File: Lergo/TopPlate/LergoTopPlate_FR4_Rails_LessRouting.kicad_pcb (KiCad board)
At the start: 2 copper layers, 164 x 146.3 mm, 74 parts, among them SW2 KEY_SWITCH, SW2 PRO MICRO

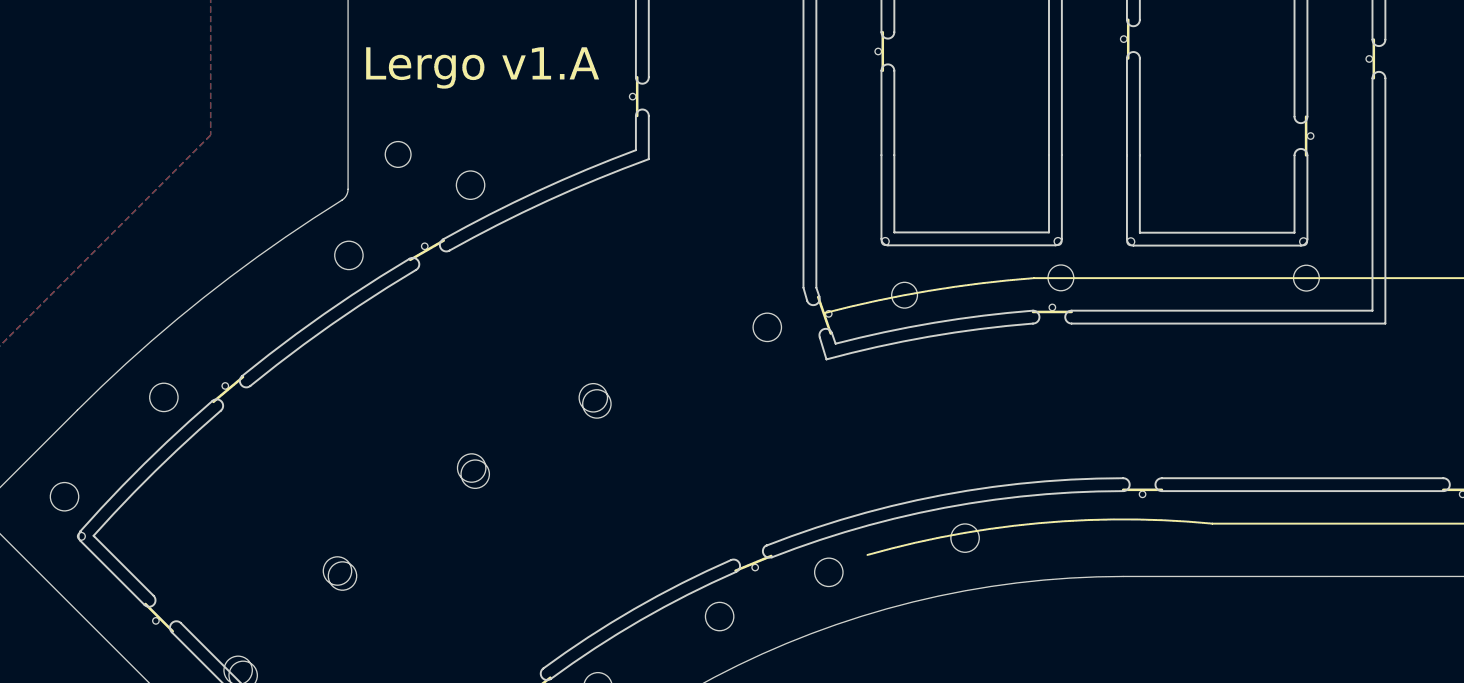
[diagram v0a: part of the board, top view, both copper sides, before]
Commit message: Fixing some issues in some FR4 top plates found while doing the Alu modifications earlier (not complete yet)
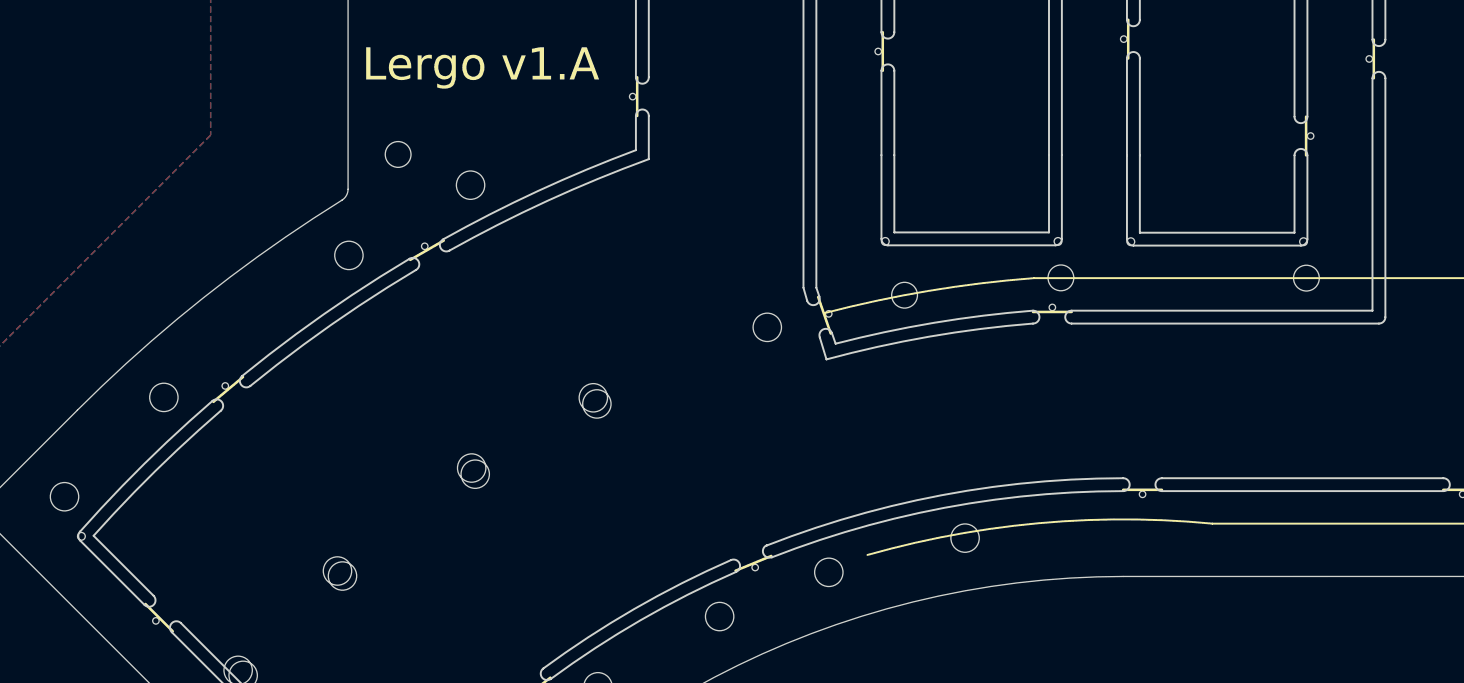
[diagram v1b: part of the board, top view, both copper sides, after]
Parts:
- moved REF** 9.48 mm to (188.1, 118.1)
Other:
- outline, holes or cut-outs redrawn

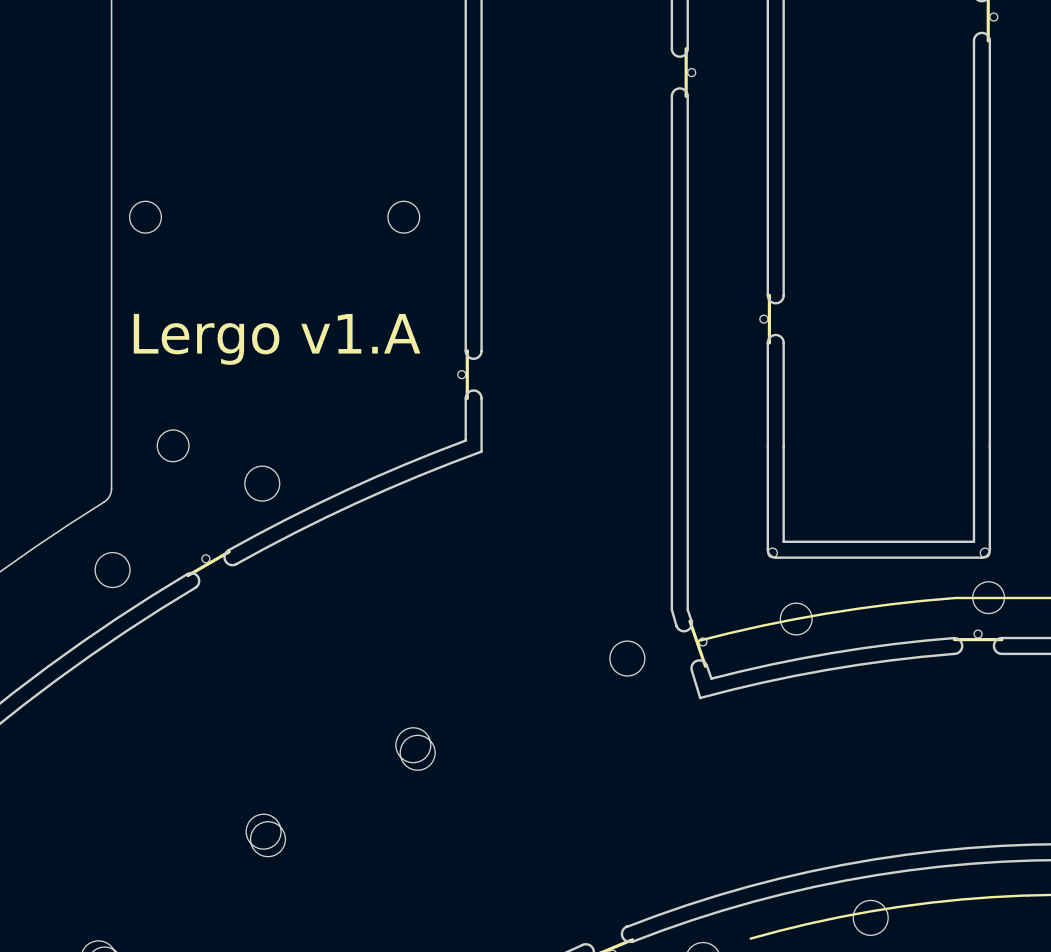
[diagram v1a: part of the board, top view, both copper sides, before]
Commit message: Finishing fixing issues in FR4 top plates
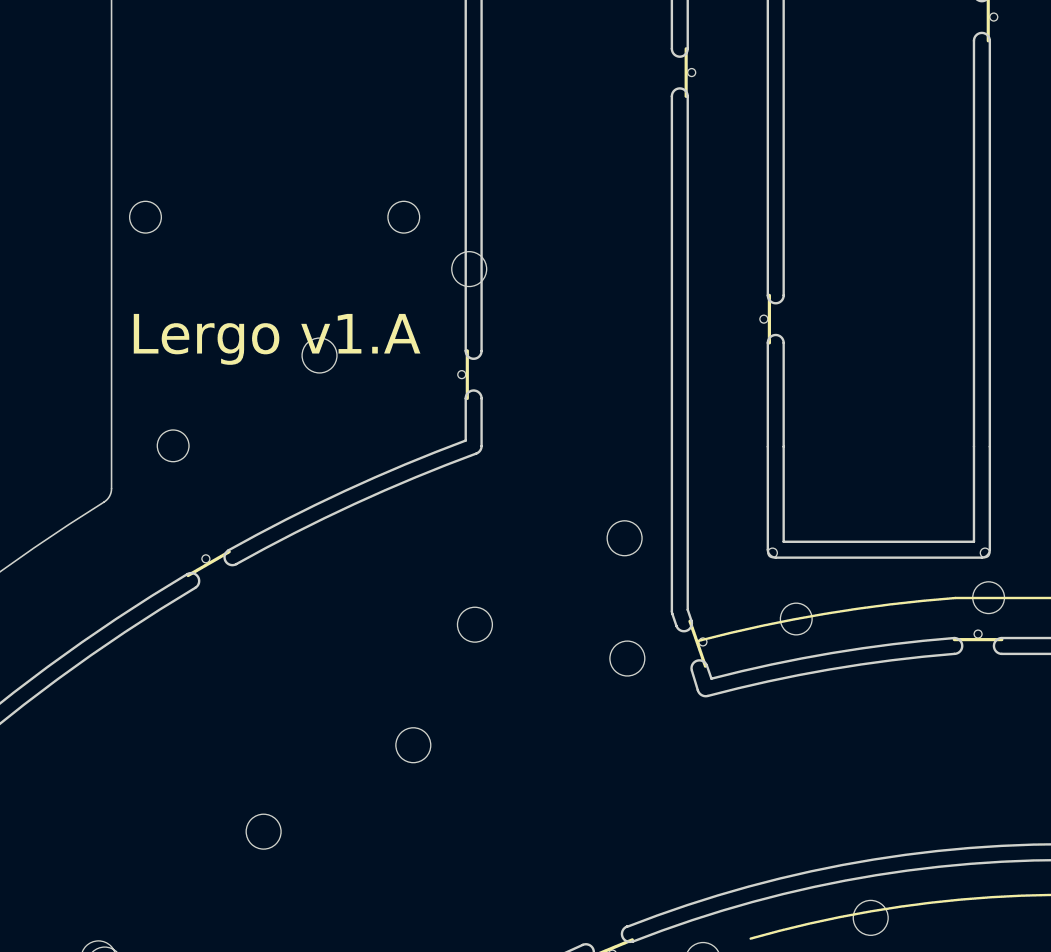
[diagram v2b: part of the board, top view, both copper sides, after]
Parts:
- moved REF** 18.8 mm to (124.3, 99.1)
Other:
- outline, holes or cut-outs redrawn
